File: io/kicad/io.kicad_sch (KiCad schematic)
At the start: 117 parts, among them J1 Conn_01x07_Pin, J2 Conn_01x02_Pin, J3 Conn_01x02_Pin, J4 Conn_01x02_Pin, J5 pcie_98, U1 ADS1261BIRHBT, U2 ESD5344D-TP, U3 TPS7A2050PDBVR, U4 TPS7A2025PDBVRr, U6 TPS65135, U7 ADP7182AUJZ-5.0, U8 ADP7182AUJZ-2.5, U9 XC6206P332MR

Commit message: Renamed the fork of kicad adc to 'io'.
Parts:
- J1: footprint adc:connector_7pins_horizontal -> io:connector_7pins_horizontal
- J2, J3, J4: footprint adc:connector_2pins_horizontal -> io:connector_2pins_horizontal
- L1: footprint adc:Inductor_C329578 -> io:Inductor_C329578
- U1: footprint adc:RHB0032E -> io:RHB0032E; symbol adc:ADS1261IRHBR -> io:ADS1261IRHBR
- U3, U4: footprint adc:SOT-23-5 -> io:SOT-23-5; symbol adc:TPS7A2050 -> io:TPS7A2050
- U6: footprint adc:WQFN-16-1EP_3x3mm_P0.5mm_EP1.68x1.68mm_ThermalVias -> io:WQFN-16-1EP_3x3mm_P0.5mm_EP1.68x1.68mm_ThermalVias; symbol adc:TPS65135 -> io:TPS65135
- U7, U8: symbol adc:ADP7182AUJZ -> io:ADP7182AUJZ

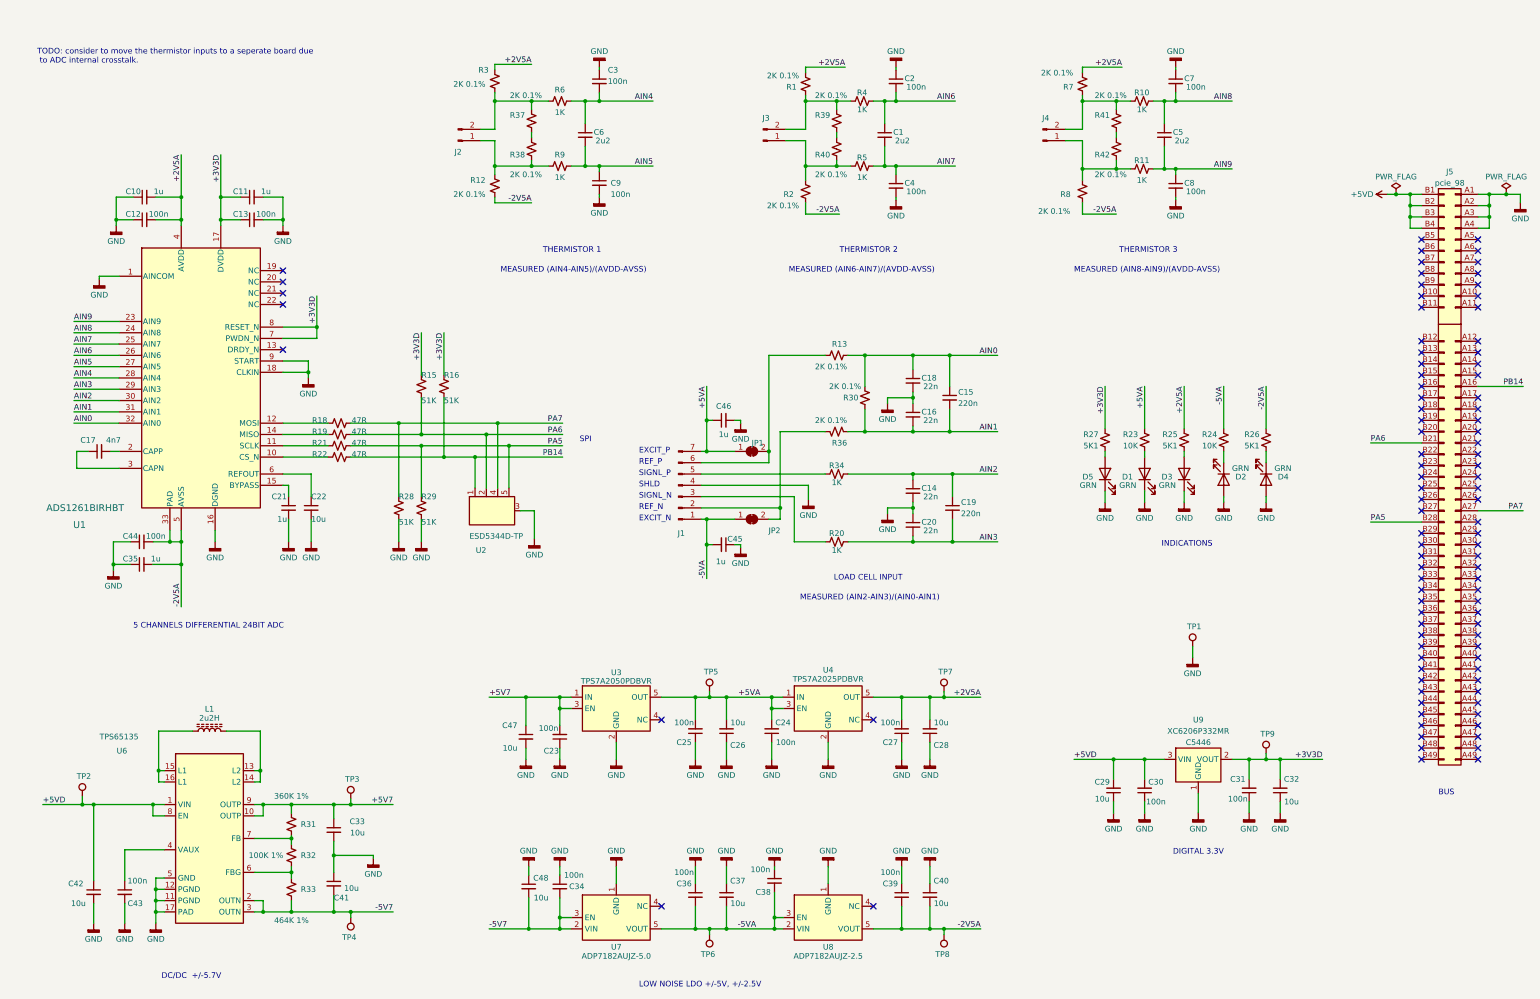
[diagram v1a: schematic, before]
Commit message: Cleaned out the io kicad from adc leftovers.
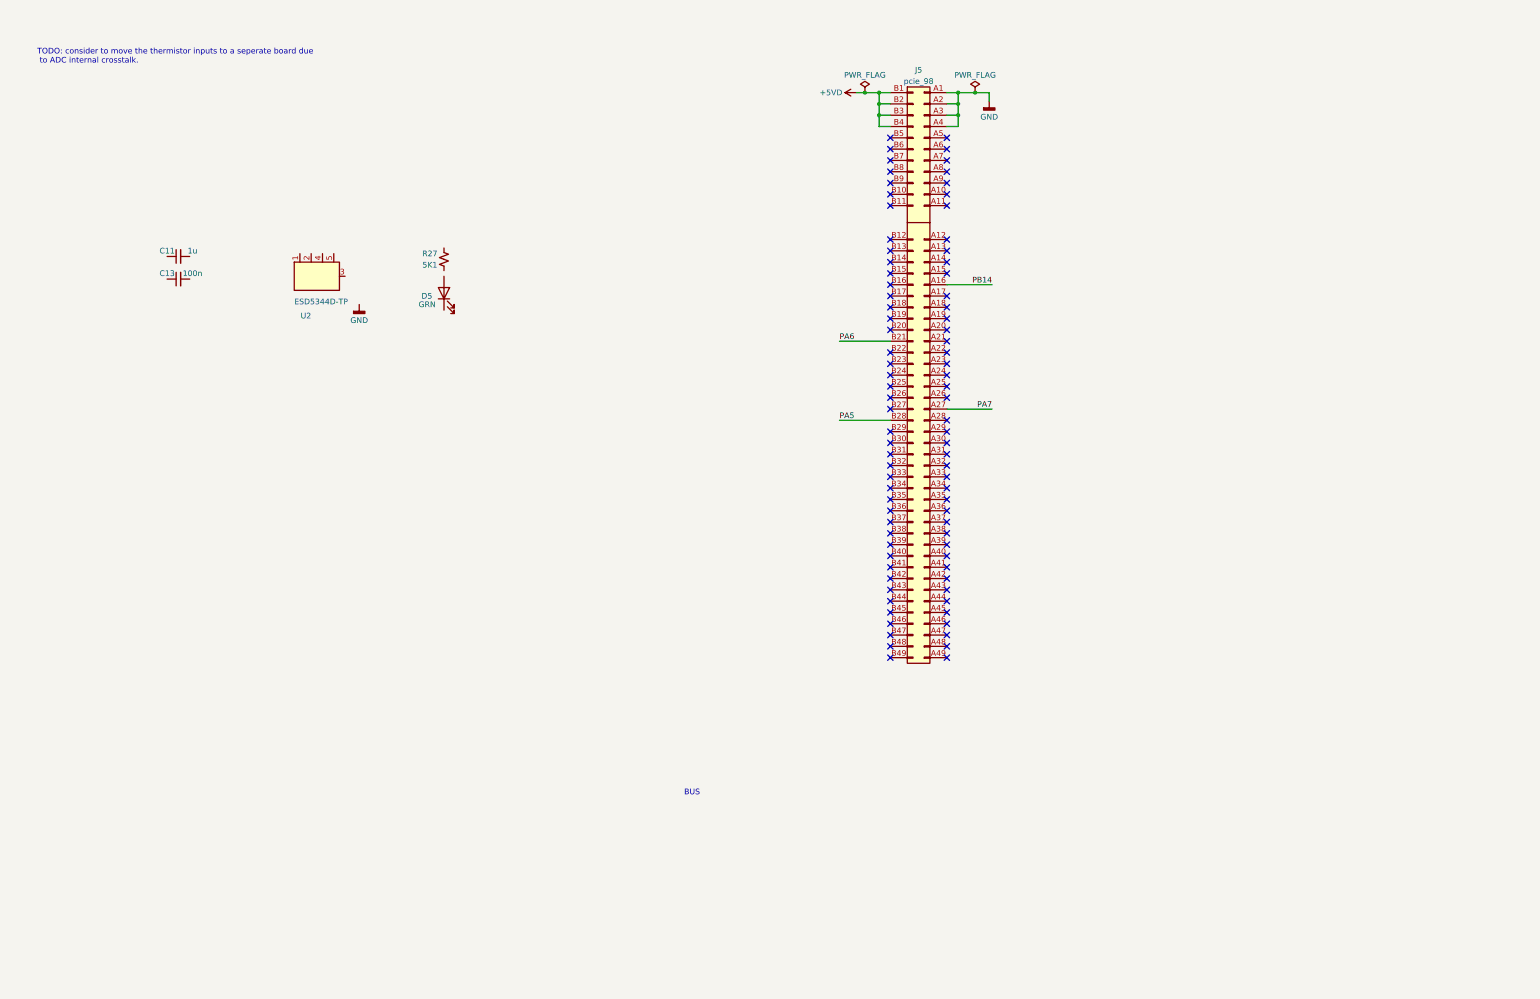
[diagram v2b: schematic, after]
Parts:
- removed C1, C5, C6: 2u2, Capacitor_SMD:C_0402_1005Metric, symbol Device:C_Small
- removed C10, C21, C35, C45, C46: 1u, Capacitor_SMD:C_0402_1005Metric, symbol Device:C_Small
- removed C12, C2, C23, C24, C25, C27, C3, C30, C31, C34, C36, C38, C39, C4, C43, C44, C7, C8, C9: 100n, Capacitor_SMD:C_0402_1005Metric, symbol Device:C_Small
- removed C14, C16, C18, C20: 22n, Capacitor_SMD:C_0402_1005Metric, symbol Device:C_Small
- removed C15, C19: 220n, Capacitor_SMD:C_0402_1005Metric, symbol Device:C_Small
- removed C17: 4n7, Capacitor_SMD:C_0402_1005Metric, symbol Device:C_Small
- removed C22, C26, C28, C29, C32, C33, C37, C40, C41, C42, C47, C48: 10u, Capacitor_SMD:C_0603_1608Metric, symbol Device:C_Small
- removed D1, D2, D3, D4: GRN, LED_SMD:LED_0603_1608Metric, symbol Device:LED
- removed J1: Conn_01x07_Pin, io:connector_7pins_horizontal, symbol Connector:Conn_01x07_Pin
- removed J2, J3, J4: Conn_01x02_Pin, io:connector_2pins_horizontal, symbol Connector:Conn_01x02_Pin
- removed JP1, JP2: SolderJumper_2_Bridged, Jumper:SolderJumper-2_P1.3mm_Bridged_Pad1.0x1.5mm, symbol Jumper:SolderJumper_2_Bridged
- removed L1: 2u2H, io:Inductor_C329578, symbol Device:L_Ferrite
- removed R1, R12, R13, R2, R3, R30, R36, R37, R38, R39, R40, R41, R42, R7, R8: 2K 0.1%, Resistor_SMD:R_0402_1005Metric, symbol Device:R_Small_US
- removed R10, R11, R20, R34, R4, R5, R6, R9: 1K, Resistor_SMD:R_0402_1005Metric, symbol Device:R_Small_US
- removed R15, R16, R28, R29: 51K, Resistor_SMD:R_0402_1005Metric, symbol Device:R_Small_US
- removed R18, R19, R21, R22: 47R, Resistor_SMD:R_0402_1005Metric, symbol Device:R_Small_US
- removed R23, R24: 10K, Resistor_SMD:R_0402_1005Metric, symbol Device:R_Small_US
- removed R25, R26: 5K1, Resistor_SMD:R_0402_1005Metric, symbol Device:R_Small_US
- removed R31: 360K 1%, Resistor_SMD:R_0402_1005Metric, symbol Device:R_Small_US
- removed R32: 100K 1%, Resistor_SMD:R_0402_1005Metric, symbol Device:R_Small_US
- removed R33: 464K 1%, Resistor_SMD:R_0402_1005Metric, symbol Device:R_Small_US
- removed TP1, TP2, TP3, TP4, TP5, TP6, TP7, TP8, TP9: TestPoint, common:Test_Pad, symbol common:TestPoint
- removed U1: ADS1261BIRHBT, io:RHB0032E, symbol io:ADS1261IRHBR
- removed U3: TPS7A2050PDBVR, io:SOT-23-5, symbol io:TPS7A2050
- removed U4: TPS7A2025PDBVRr, io:SOT-23-5, symbol io:TPS7A2050
- removed U6: TPS65135, io:WQFN-16-1EP_3x3mm_P0.5mm_EP1.68x1.68mm_ThermalVias, symbol io:TPS65135
- removed U7: ADP7182AUJZ-5.0, Package_TO_SOT_SMD:TSOT-23-5, symbol io:ADP7182AUJZ
- removed U8: ADP7182AUJZ-2.5, Package_TO_SOT_SMD:TSOT-23-5, symbol io:ADP7182AUJZ
- removed U9: XC6206P332MR, Package_TO_SOT_SMD:SOT-23-3, symbol breakout:XC6206P332MR
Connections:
- net GND: no longer C11.2, C13.2, D5.1 (K), U2.3 (GND)
- net PA5: no longer U2.5 (D4)
- net PA6: no longer U2.2 (D2)
- net PA7: no longer U2.4 (D3)
- net PB14: no longer U2.1 (D1)
- net at D5.2 (A): no longer R27.2
- removed net +3V3D: C11.1, C13.1, R27.1
- no-connect marks 95 -> 86
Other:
- note removed: "5 CHANNELS DIFFERENTIAL 24BIT ADC"
- note removed: "DC/DC +/-5.7V"
- note removed: "DIGITAL 3.3V"
- note removed: "EXCIT_N"
- note removed: "EXCIT_P"
- note removed: "INDICATIONS"
- note removed: "LOAD CELL INPUT"
- note removed: "LOW NOISE LDO +/-5V, +/-2.5V"
- note removed: "MEASURED (AIN2-AIN3)/(AIN0-AIN1)"
- note removed: "MEASURED (AIN4-AIN5)/(AVDD-AVSS)"
- note removed: "MEASURED (AIN6-AIN7)/(AVDD-AVSS)"
- note removed: "MEASURED (AIN8-AIN9)/(AVDD-AVSS)"
- note removed: "REF_N"
- note removed: "REF_P"
- note removed: "SHLD"
- note removed: "SIGNL_N"
- note removed: "SIGNL_P"
- note removed: "SPI"
- note removed: "THERMISTOR 1"
- note removed: "THERMISTOR 2"
- note removed: "THERMISTOR 3"
- moved on the sheet: C11, C13, D5, J5, R27, U2

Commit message: IO board schematic in progress.
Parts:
- added C1, C3, C4, C8, C9: 10u, Capacitor_SMD:C_0402_1005Metric, symbol Device:C_Small
- added C10: 1u, Capacitor_SMD:C_0402_1005Metric, symbol Device:C_Small
- added C12, C2, C5, C6, C7: 100n, Capacitor_SMD:C_0402_1005Metric, symbol Device:C_Small
- added D1: GRN, LED_SMD:LED_0603_1608Metric, symbol Device:LED
- added J1: Conn_01x04_Pin, symbol Connector:Conn_01x04_Pin
- added R1, R2, R4: R_US, symbol Device:R_US
- added R5, R6: 0R, symbol Device:R_US
- added R7: 5K1, Resistor_SMD:R_0402_1005Metric, symbol Device:R_Small_US
- added U1, U6: XC6206P332MR, Package_TO_SOT_SMD:SOT-89-3, symbol common:XC6206P332MR
- added U3: B0505MT-1WR4, symbol io:isolated_dc_dc
- added U4: ADuM1201AR, Package_SO:SOIC-8_3.9x4.9mm_P1.27mm, symbol Isolator:ADuM1201AR
- added U5: ESD5344D-TP, common:Diodes_UDFN-10_1.0x2.5mm_P0.5mm, symbol common:ESD5344D
- C11: value 1u -> 100n; LCSC C52923 -> (none)
- C13: LCSC C1525 -> (none)
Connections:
- net GND: now also C11.1, C4.1, C5.1, C6.1, C7.1, C8.1, C9.1, D1.1 (K), U3.1 (GND), U3.2 (GND), U4.5 (GND2), U5.3 (GND), U6.1 (GND)
- net at U2.1 (D1): now also C10.2, C12.2, J1.1 (Pin_1), R4.2, R5.1, R6.1, U4.1 (VDD1)
- net at U2.2 (D2): now also R1.2, U4.2 (VOA)
- net GND1: now reaches U2.3 (GND)
- net GND1: now also C13.1, D5.1 (K), C1.1, C10.1, C12.1, C2.1, C3.1, J1.4 (Pin_4), U1.1 (GND), U3.6 (OUTN), U3.7 (OUTN), U4.4 (GND1)
- net at U2.4 (D3): now also R2.2, U4.3 (VIB)
- net +5VF: now reaches C13.2
- net +5VF: now also C1.2, R5.2, U1.3 (VIN), U3.8 (OUTP)
- net +3.3V: now reaches C11.2
- net +3.3V: now also C7.2, C8.2, R7.1, U4.8 (VDD2), U6.2 (VOUT)
- net at D5.2 (A): now also R27.2
- net +3V3F: now reaches R27.1
- net +3V3F: now also C2.2, C3.2, R6.2, U1.2 (VOUT)
- net +5VD renamed +5V
- net +5V: now also C4.2, C5.2, C6.2, C9.2, U3.13 (IN), U3.14 (IN), U6.3 (VIN)
- new net: J1.3 (Pin_3), R2.1, R4.1
- new net: D1.2 (A), R7.2
- new net: J1.2 (Pin_2), R1.1
- no-connect marks 86 -> 87
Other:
- note added: "FLOATING POWER SUPPLY"
- note removed: "TODO: consider to move the thermistor inputs to a seperate board due to ADC internal crosstalk."
- title: ADS1261B ADC BOARD -> IO BOARD
- moved on the sheet: C13, D5, R27, U2
